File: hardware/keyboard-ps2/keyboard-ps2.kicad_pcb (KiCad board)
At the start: 2 copper layers, 87.6 x 68.6 mm, 35 parts, among them J1 JP***, J2 PS2_CONN, U1 74HC595, U10 74HC595, U11 74HC595, U12 ATMEGA328P, U2 74HC595, U3 74HC595, U4 74HC595, U5 74HC595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

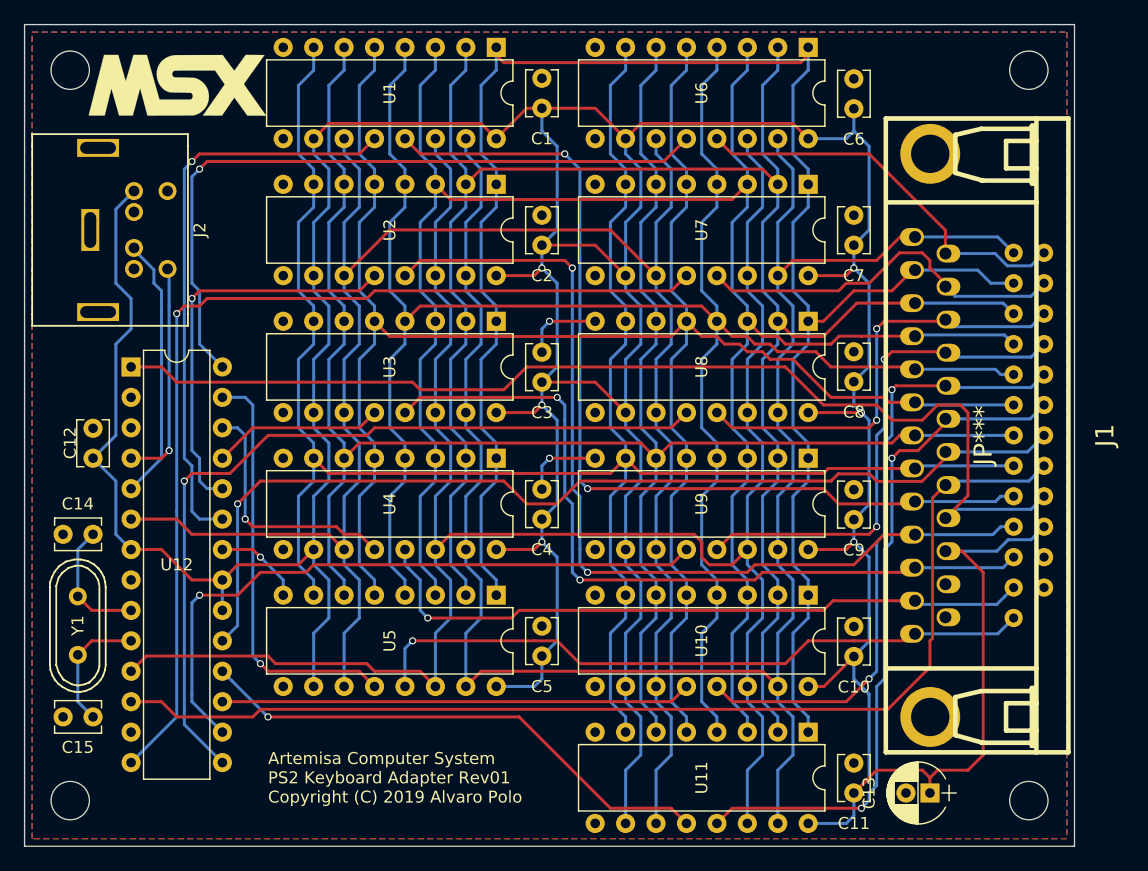
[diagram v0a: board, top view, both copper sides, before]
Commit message: Shorten the PCB and the DB25 connector in PS2 Adapter
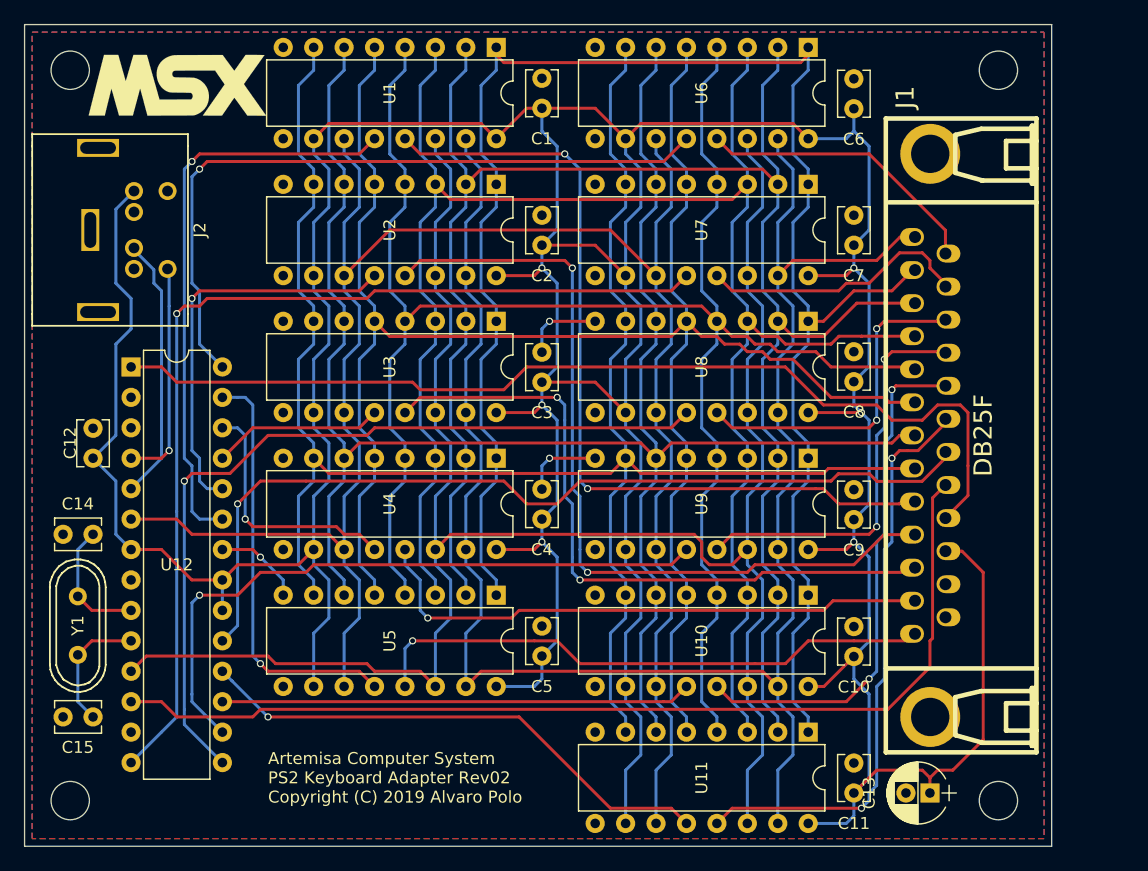
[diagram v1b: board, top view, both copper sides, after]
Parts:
- J1: value JP*** -> DB25F
- moved REF** 2.54 mm to (176.5, 68.6)
- moved REF** 2.54 mm to (176.5, 129.5)
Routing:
- net ~: track 427.6 -> 417.8 mm
- net /~RSL5: track 33.3 -> 24.2 mm
- net /~RSL6: track 31.6 -> 22.6 mm
- net /~RESET: track 92.6 -> 83.6 mm
- net /~RSL3: track 56.7 -> 47.8 mm
- net /~RSL7: track 36.7 -> 27.8 mm
- net /~KANALOCK: track 93.6 -> 84.7 mm
- net /~RSL8: track 42.6 -> 33.8 mm
- net /~CAPSLOCK: track 84.0 -> 75.2 mm
- net /~RSL4: track 56.6 -> 47.8 mm
- net /KBCOL0: track 161.0 -> 152.2 mm
- net /~RSL9: track 52.3 -> 43.5 mm
- net /~RSL10: track 57.6 -> 48.9 mm
- net /KBCOL1: track 159.5 -> 150.9 mm
- net /~RSL2: track 66.2 -> 57.6 mm
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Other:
- board size 87.6 x 68.6 mm -> 85.7 x 68.6 mm
- board text added: "Artemisa Computer System PS2 Keyboard Adapter Rev02 Copyright (C) 2019 Alvaro Polo"
- board text removed: "Artemisa Computer System PS2 Keyboard Adapter Rev01 Copyright (C) 2019 Alvaro Polo"

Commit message: Increse width of power tracks in PS2 Keyboard Adapter
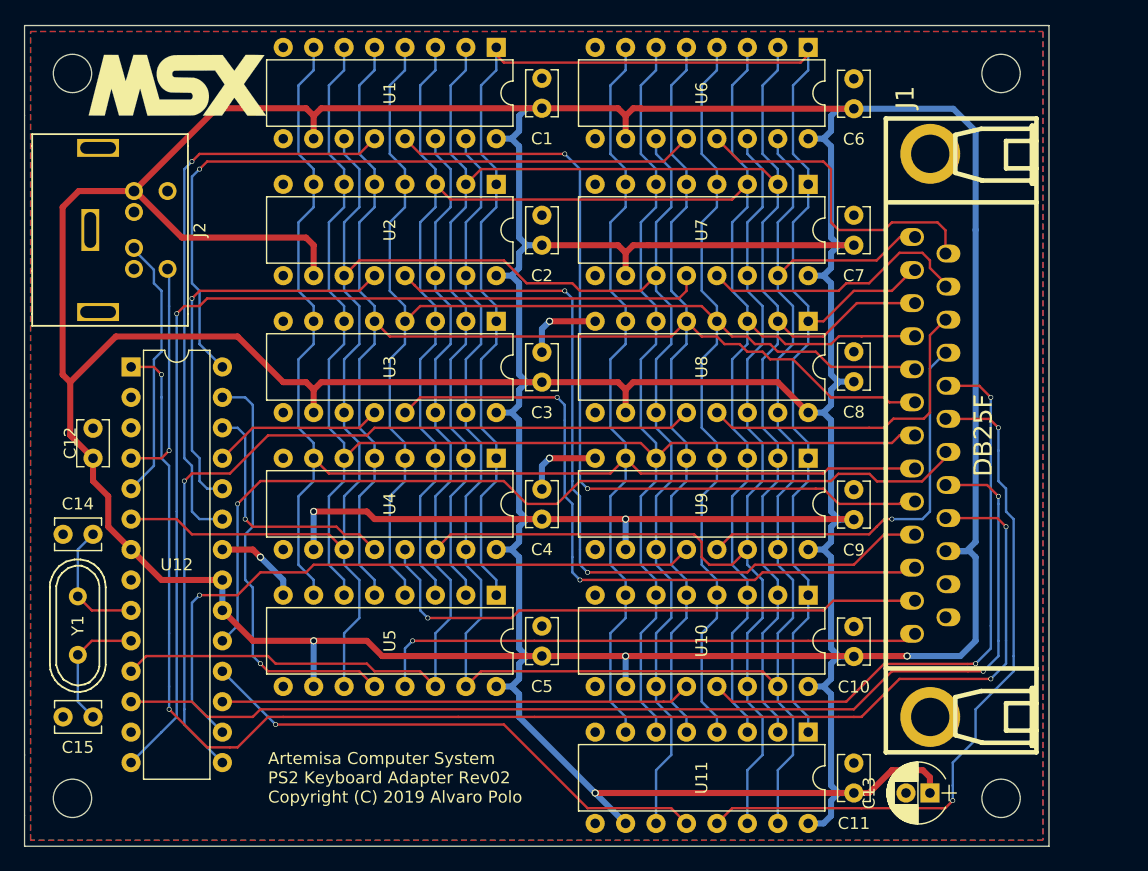
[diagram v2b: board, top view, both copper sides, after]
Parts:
- moved REF** 0.35 mm to (176.8, 68.8)
- moved REF** 0.33 mm to (99.2, 68.8)
- moved REF** 0.29 mm to (176.8, 129.3)
- moved REF** 0.27 mm to (99.2, 129.3)
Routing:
- net ~: track 417.8 -> 607.4 mm
- net /~RESET: track 83.6 -> 121.8 mm, vias 0 -> 4
- net /~RSL10: track 48.9 -> 58.9 mm
- net /~KANALOCK: track 84.7 -> 93.2 mm, vias 0 -> 2
- net /~RSL9: track 43.5 -> 50.4 mm
- net /~RSL5: track 24.2 -> 27.3 mm
- net /~RSL1: track 69.3 -> 66.8 mm
- net /~RSL4: track 47.8 -> 46.3 mm
- net /SHCP: track 160.4 -> 159.3 mm
- net /~RSL8: track 33.8 -> 32.9 mm, vias 2 -> 1
- net /STCP6: track 82.9 -> 83.6 mm
- net /~RSL7: track 27.8 -> 27.1 mm, vias 2 -> 0
- net /STCP4: track 35.0 -> 35.5 mm
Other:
- board size 85.7 x 68.6 mm -> 85.5 x 68.5 mm
- net class Default: clearance 0.2 -> 0.2032; trace_width 0.25 -> 0.2032; via_dia 0.6 -> 0.4064; via_drill 0.4 -> 0.3048
- net class Power added: clearance 0.254, trace_width 0.508, via_dia 0.6096, via_drill 0.4064
- rule trace_clearance: 0.2 -> 0.2032
- rule trace_min: 0.2 -> 0.1524
- rule via_min_drill: 0.3 -> 0.3048
- rule via_min_size: 0.4 -> 0.4064

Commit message: [ps2-adapter] Add 2 jumpers for KB layout selection
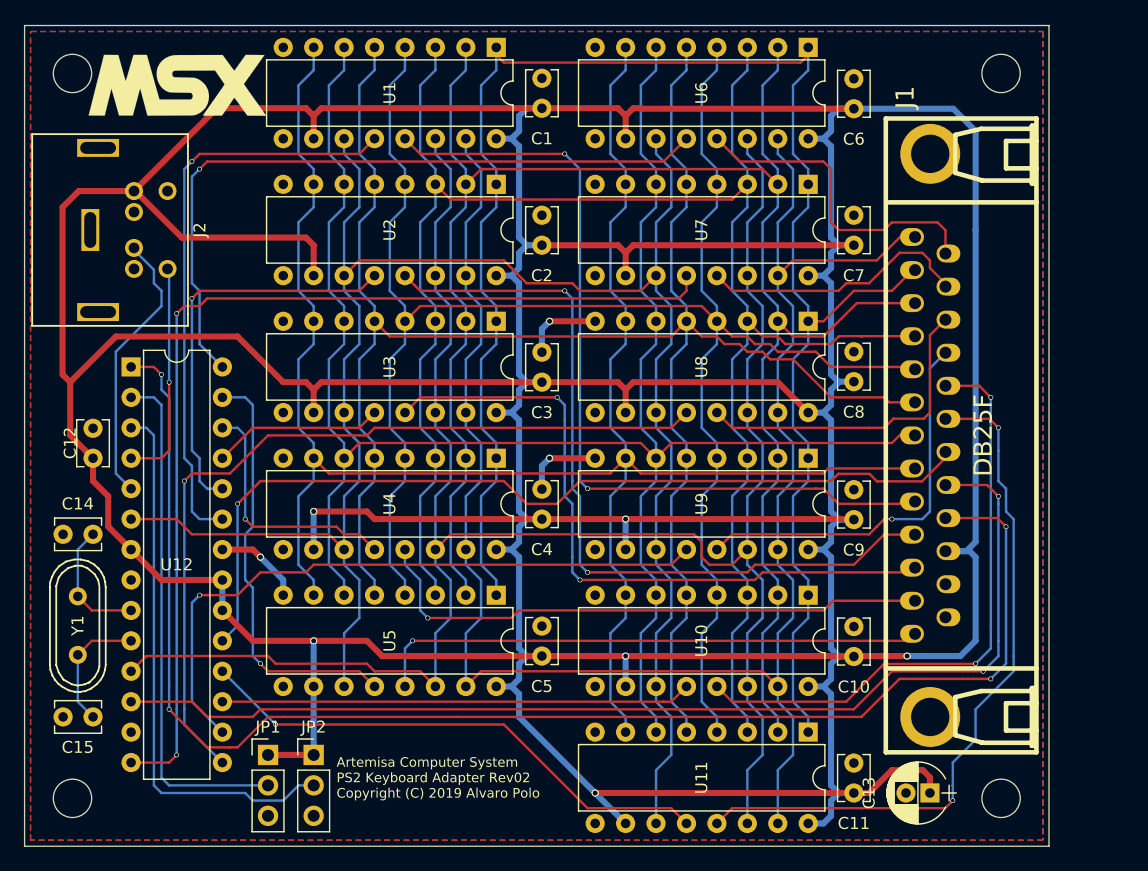
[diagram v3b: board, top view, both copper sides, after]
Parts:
- added JP1: Jumper, artemisa:Jumper, F.Cu at (115.6, 125.7)
- added JP2: Jumper, artemisa:Jumper, F.Cu at (119.4, 125.7)
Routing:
- net Net-(JP2-Pad2): track 0.00 -> 45.8 mm
- net Net-(JP1-Pad2): track 0.00 -> 43.1 mm
- net ~: track 607.4 -> 616.9 mm
- net /STCP6: track 83.6 -> 85.5 mm, vias 1 -> 2
- net Net-(J2-Pad1): track 22.1 -> 23.1 mm

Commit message: [ps2-adapter] Add changelog file
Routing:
- net ~: track 616.9 -> 636.5 mm
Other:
- board text added: "Artemisa Computer System PS2 Keyboard Adapter Rev2 Copyright (C) 2019 Alvaro Polo"
- board text removed: "Artemisa Computer System PS2 Keyboard Adapter Rev02 Copyright (C) 2019 Alvaro Polo"
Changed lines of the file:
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@@
     (thickness 1.6)
     (drawings 8)
-    (tracks 1091)
+    (tracks 1095)
     (zones 0)
     (modules 37)
@@
   (gr_line (start 95.25 64.85) (end 180.75 64.85) (layer Edge.Cuts) (width 0.1))
   (gr_line (start 95.25 133.35) (end 180.75 133.35) (layer Edge.Cuts) (width 0.1))
-  (gr_text "Artemisa Computer System\nPS2 Keyboard Adapter Rev02\nCopyright (C) 2019 Alvaro Polo" (at 121.285 127.635) (layer F.SilkS)
+  (gr_text "Artemisa Computer System\nPS2 Keyboard Adapter Rev2\nCopyright (C) 2019 Alvaro Polo" (at 121.285 127.635) (layer F.SilkS)
     (effects (font (size 0.8 0.8) (thickness 0.12)) (justify left))
   )
@@
   (segment (start 119.38 120.015) (end 119.38 125.73) (width 0.508) (layer B.Cu) (net 2))
   (segment (start 119.38 125.73) (end 115.57 125.73) (width 0.508) (layer F.Cu) (net 2))
+  (segment (start 138.43 83.185) (end 137.16 83.185) (width 0.508) (layer F.Cu) (net 2))
+  (segment (start 137.16 83.185) (end 136.525 82.55) (width 0.508) (layer F.Cu) (net 2))
+  (segment (start 120.015 82.55) (end 119.38 83.185) (width 0.508) (layer F.Cu) (net 2))
+  (segment (start 136.525 82.55) (end 120.015 82.55) (width 0.508) (layer F.Cu) (net 2))
   (segment (start 100.86594 113.665) (end 99.695 112.49406) (width 0.2032) (layer F.Cu) (net 3))
   (segment (start 104.14 113.665) (end 100.86594 113.665) (width 0.2032) (layer F.Cu) (net 3))

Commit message: [ps2-adapter] Fix capacitor values for clock circuit
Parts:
- C14, C15: value 22pF -> 33pF
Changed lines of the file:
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@@
       (effects (font (size 1 1) (thickness 0.15)))
     )
-    (fp_text value 22pF (at 5.08 0 270) (layer F.Fab)
+    (fp_text value 33pF (at 5.08 0 270) (layer F.Fab)
       (effects (font (size 1 1) (thickness 0.15)))
     )
@@
       (effects (font (size 1 1) (thickness 0.15)))
     )
-    (fp_text value 22pF (at 4.445 -0.635 90) (layer F.Fab)
+    (fp_text value 33pF (at 4.445 -0.635 90) (layer F.Fab)
       (effects (font (size 1 1) (thickness 0.15)))
     )

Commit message: [ps2-adapter] Set board settings to match JCLPCB design rules
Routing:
- net ~: vias 6 -> 5
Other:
- net class Default: via_dia 0.4064 -> 0.6; via_drill 0.3048 -> 0.3
- net class Power: via_dia 0.6096 -> 1; via_drill 0.4064 -> 0.5
- rule via_min_drill: 0.3048 -> 0.3
- rule via_min_size: 0.4064 -> 0.6

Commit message: Update changelogs and revision numbers of all PCBs
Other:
- board text added: "Artemisa Computer System PS2 Keyboard Adapter Rev3 Copyright (C) 2019 Alvaro Polo"
- board text removed: "Artemisa Computer System PS2 Keyboard Adapter Rev2 Copyright (C) 2019 Alvaro Polo"
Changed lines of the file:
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@@
   (gr_line (start 95.25 64.85) (end 180.75 64.85) (layer Edge.Cuts) (width 0.1))
   (gr_line (start 95.25 133.35) (end 180.75 133.35) (layer Edge.Cuts) (width 0.1))
-  (gr_text "Artemisa Computer System\nPS2 Keyboard Adapter Rev2\nCopyright (C) 2019 Alvaro Polo" (at 121.285 127.635) (layer F.SilkS)
+  (gr_text "Artemisa Computer System\nPS2 Keyboard Adapter Rev3\nCopyright (C) 2019 Alvaro Polo" (at 121.285 127.635) (layer F.SilkS)
     (effects (font (size 0.8 0.8) (thickness 0.12)) (justify left))
   )
